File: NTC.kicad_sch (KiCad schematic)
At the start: 16 parts, among them U3 LM1117GS-3.3, U4 LMV331

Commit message: Тестовая версия
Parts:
- gave numbers to parts that had none: 1
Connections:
- net E1 renamed E3
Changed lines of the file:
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@@
     (stroke (width 0) (type default) (color 0 0 0 0))
   )
-  (global_label "E1" (shape input) (at 62.484 96.139 180) (fields_autoplaced)
+  (global_label "E3" (shape input) (at 62.484 96.139 180) (fields_autoplaced)
     (effects (font (size 1.27 1.27)) (justify right))
     (property "Intersheet References" "${INTERSHEET_REFS}" (id 0) (at 57.7123 96.0596 0)
@@
   (symbol (lib_id "Isolator:ADuM1200AR") (at 172.339 101.219 0) (unit 1)
     (in_bom yes) (on_board yes) (fields_autoplaced)
-    (property "Reference" "U?" (id 0) (at 172.339 88.519 0))
+    (property "Reference" "U5" (id 0) (at 172.339 88.519 0))
     (property "Value" "ADuM1200AR" (id 1) (at 172.339 91.059 0))
     (property "Footprint" "Package_SO:SOIC-8_3.9x4.9mm_P1.27mm" (id 2) (at 172.339 111.379 0)

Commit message: Сохранил изменения в схеме
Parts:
- removed U4: LMV331, Package_TO_SOT_SMD:SOT-23-5, symbol Comparator:LMV331
- added U11: LMV7219M5, Package_TO_SOT_SMD:SOT-23-5, symbol Comparator:LMV7219M5
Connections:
- net +3.3VA: now also U11.5 (V+)
- net GND1: now also U11.2 (V-)
- net NTC1: now also U11.4 (-)
- net at C33.1, R25.1, R26.2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: now also U11.3 (+)
- net at C33.2, R27.2, R28.1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: now also U11.1

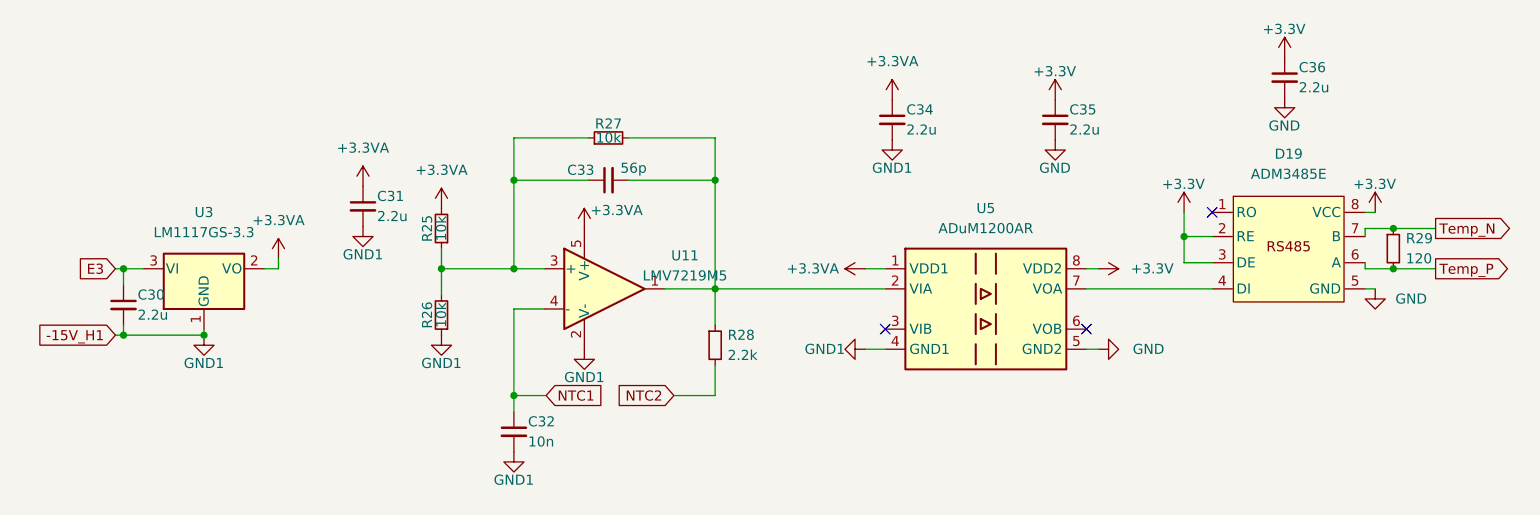
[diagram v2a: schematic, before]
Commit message: Убрал питание 3.3В
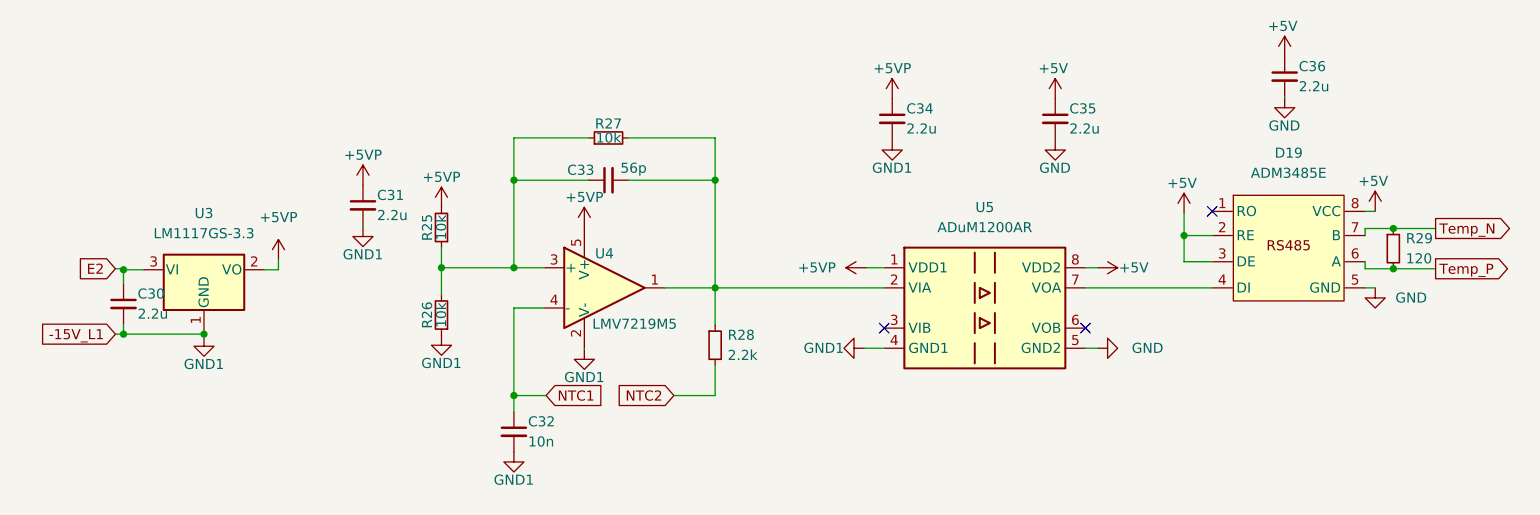
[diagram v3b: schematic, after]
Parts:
- renumbered U11 to U4
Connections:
- net +3.3VA renamed +5VP
- net +3V3 renamed +5V
- net E3 renamed E2

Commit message: Развел все дорожки
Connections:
- net E2 renamed E3
- net GND1 renamed -15V_H
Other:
- moved on the sheet: C31, C34

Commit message: VER2.0 Отправил в резонит
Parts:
- U3: value LM1117GS-3.3 -> LM1117GS-5.0
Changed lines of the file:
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@@
 			)
 		)
-		(property "Description" ""
+		(property "Description" "ADuM1200AR"
 			(at 172.085 100.965 0)
 			(effects
@@
 			)
 		)
-		(property "Description" ""
+		(property "Description" "LMV7219M5"
 			(at 124.46 98.425 0)
 			(effects
@@
 			)
 		)
-		(property "Value" "LM1117GS-3.3"
+		(property "Value" "LM1117GS-5.0"
 			(at 73.66 91.948 0)
 			(effects
@@
 			)
 		)
-		(property "Description" ""
+		(property "Description" "LM1117GS-5.0"
 			(at 73.66 96.52 0)
 			(effects
@@
 			)
 		)
-		(property "Description" ""
+		(property "Description" "ADM3485E"
 			(at 210.312 84.328 0)
 			(effects

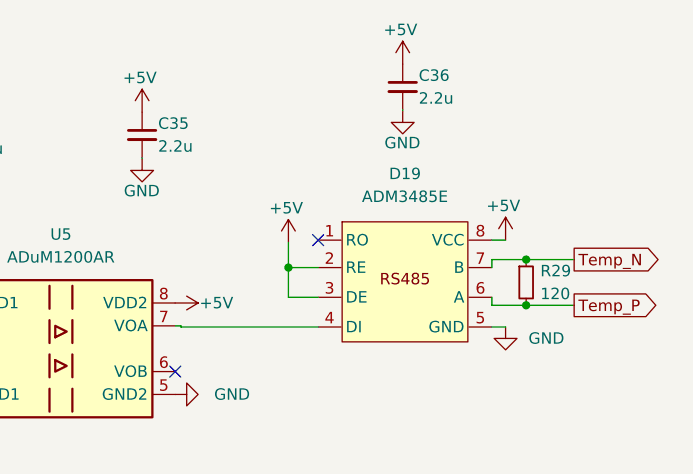
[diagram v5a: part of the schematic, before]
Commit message: Изменения: изменил BOM, сделал заказ
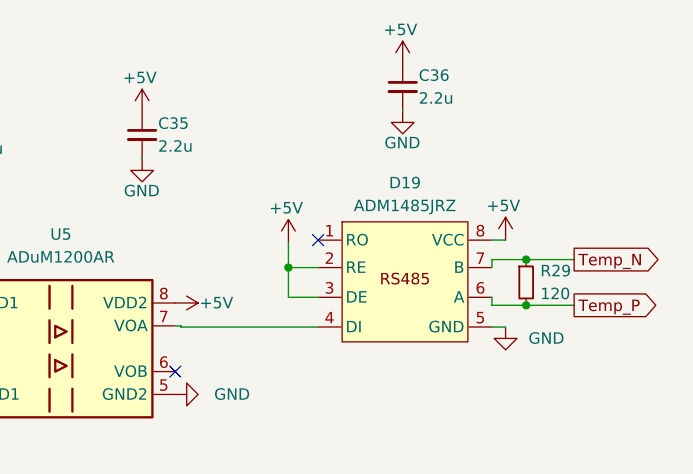
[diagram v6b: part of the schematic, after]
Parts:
- D19: value ADM3485E -> ADM1485JRZ
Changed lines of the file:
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@@
 		(fields_autoplaced yes)
 		(property "Reference" "D19"
-			(at 210.312 81.534 0)
+			(at 210.312 82.55 0)
 			(effects
 				(font
@@
 			)
 		)
-		(property "Value" "ADM3485E"
-			(at 210.312 84.074 0)
+		(property "Value" "ADM1485JRZ"
+			(at 210.312 85.09 0)
 			(effects
 				(font

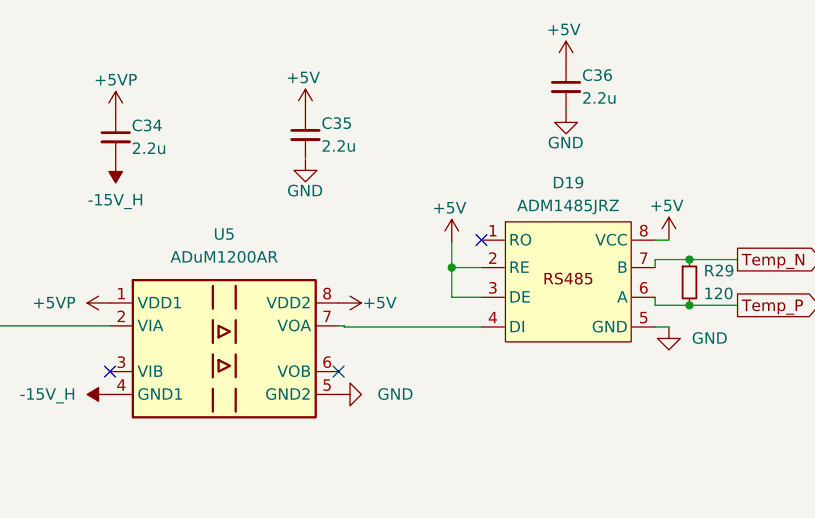
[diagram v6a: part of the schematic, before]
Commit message: VER2_Test: добавил новый BOM и в схеме заменил названия компонентов
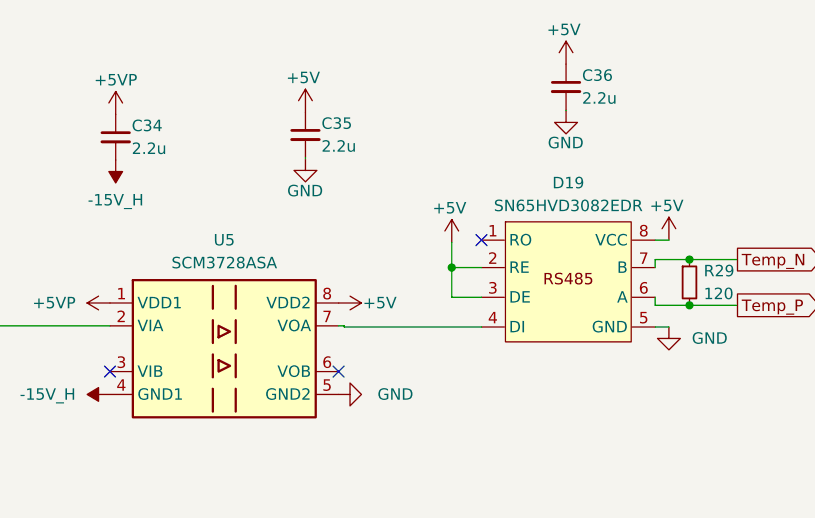
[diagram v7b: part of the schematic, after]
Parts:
- D19: value ADM1485JRZ -> SN65HVD3082EDR
- U5: value ADuM1200AR -> SCM3728ASA
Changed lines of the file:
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@@
 		(fields_autoplaced yes)
 		(property "Reference" "U5"
-			(at 172.085 88.265 0)
-			(effects
-				(font
-					(size 1.27 1.27)
-				)
-			)
-		)
-		(property "Value" "ADuM1200AR"
-			(at 172.085 90.805 0)
+			(at 172.085 88.9 0)
+			(effects
+				(font
+					(size 1.27 1.27)
+				)
+			)
+		)
+		(property "Value" "SCM3728ASA"
+			(at 172.085 91.44 0)
 			(effects
 				(font
@@
 			)
 		)
-		(property "Value" "ADM1485JRZ"
+		(property "Value" "SN65HVD3082EDR"
 			(at 210.312 85.09 0)
 			(effects
